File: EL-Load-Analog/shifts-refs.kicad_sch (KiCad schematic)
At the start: 44 parts, among them U501 TL431DBZ, U502 TL074, U503 TL074, U504 TL072

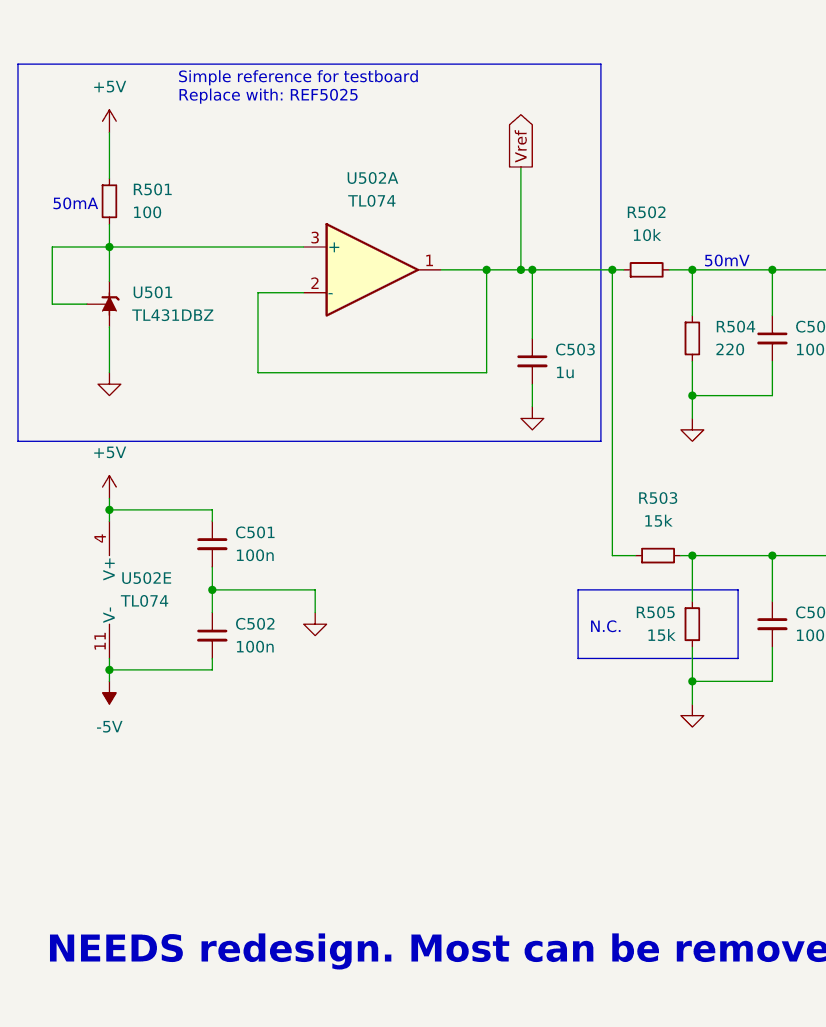
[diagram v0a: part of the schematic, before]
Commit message: Put REF2025 in place, added LICENSES and .gitignore
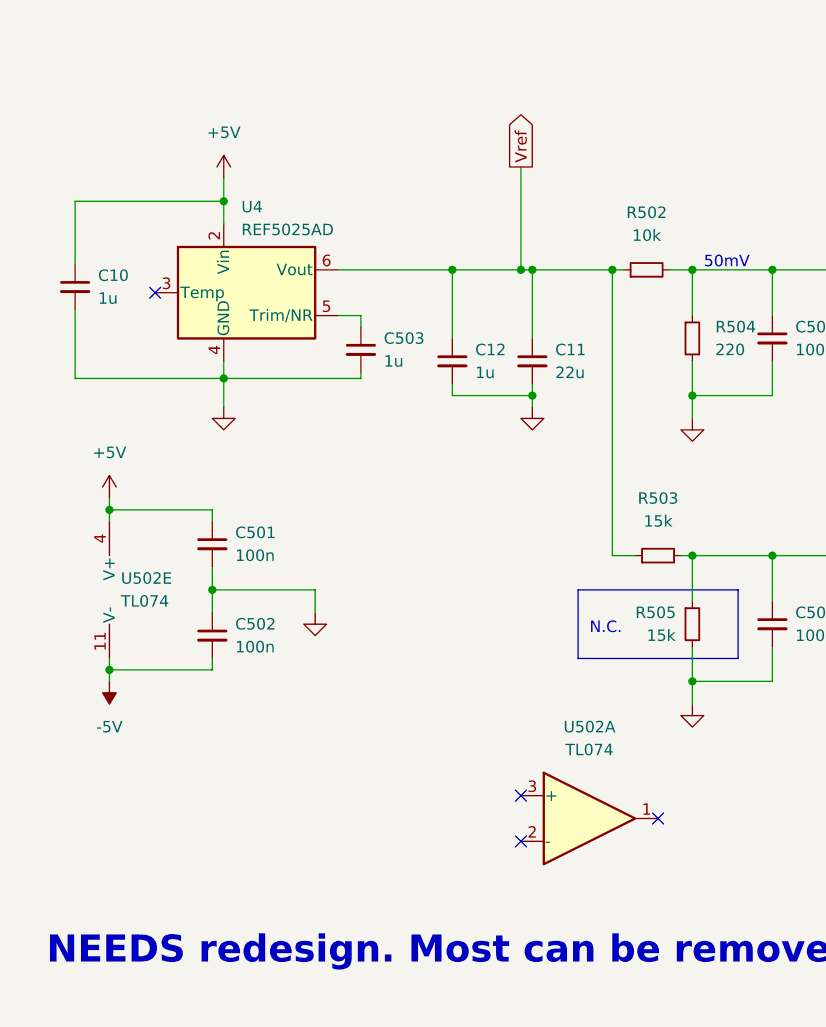
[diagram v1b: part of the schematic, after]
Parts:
- removed R501: 100, Resistor_SMD:R_0805_2012Metric_Pad1.20x1.40mm_HandSolder, symbol Device:R_Small
- removed U501: TL431DBZ, Package_TO_SOT_SMD:SOT-23, symbol Reference_Voltage:TL431DBZ
- added C10, C12: 1u, Capacitor_SMD:C_0805_2012Metric_Pad1.18x1.45mm_HandSolder, symbol Device:C_Small
- added C11: 22u, Capacitor_SMD:C_0805_2012Metric_Pad1.18x1.45mm_HandSolder, symbol Device:C_Small
- added U4: REF5025AD, Package_SO:SOIC-8_3.9x4.9mm_P1.27mm, symbol Reference_Voltage:REF5025AD
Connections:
- net +5V: now also C10.1, U4.2 (Vin)
- net GND: now also C10.2, C11.2, C12.2, U4.4 (GND)
- net Vref: now also C11.1, C12.1, U4.6 (Vout); no longer C503.1, U502.1, U502.2 (-)
- new net: C503.1, U4.5 (Trim/NR)
- no-connect marks 0 -> 4
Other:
- note removed: "50mA"
- note removed: "Simple reference for testboard Replace with: REF5025"
- moved on the sheet: C503, U502A

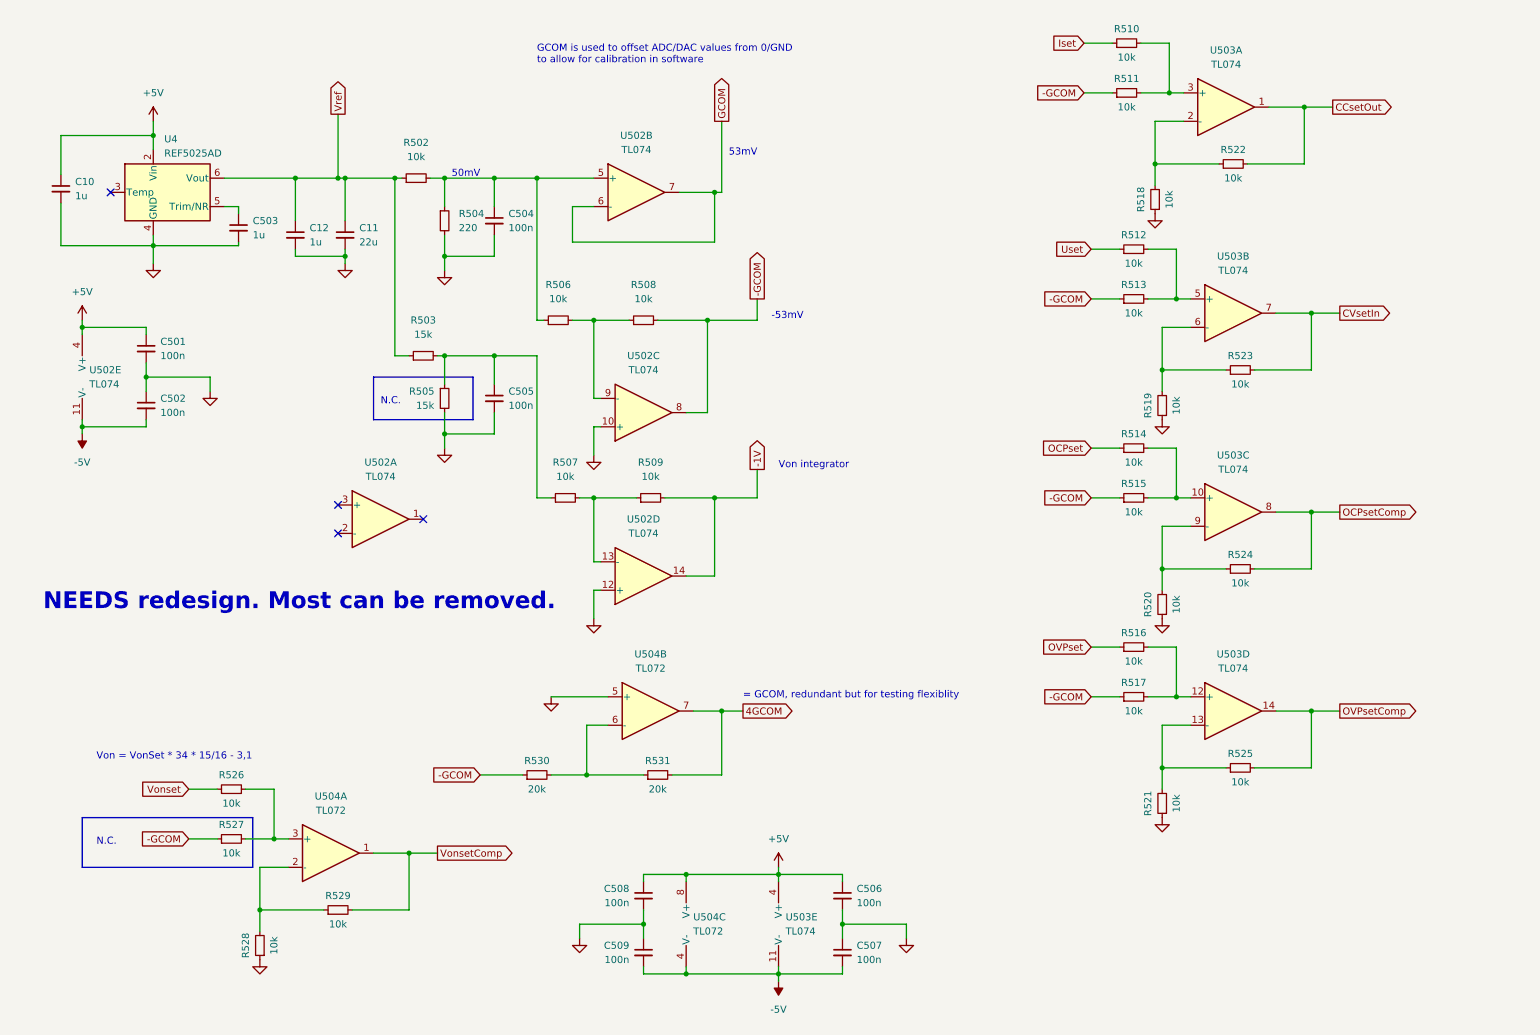
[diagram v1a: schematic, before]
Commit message: Major Analog PCB update DAC/ADC + connectors included, fan IC removed
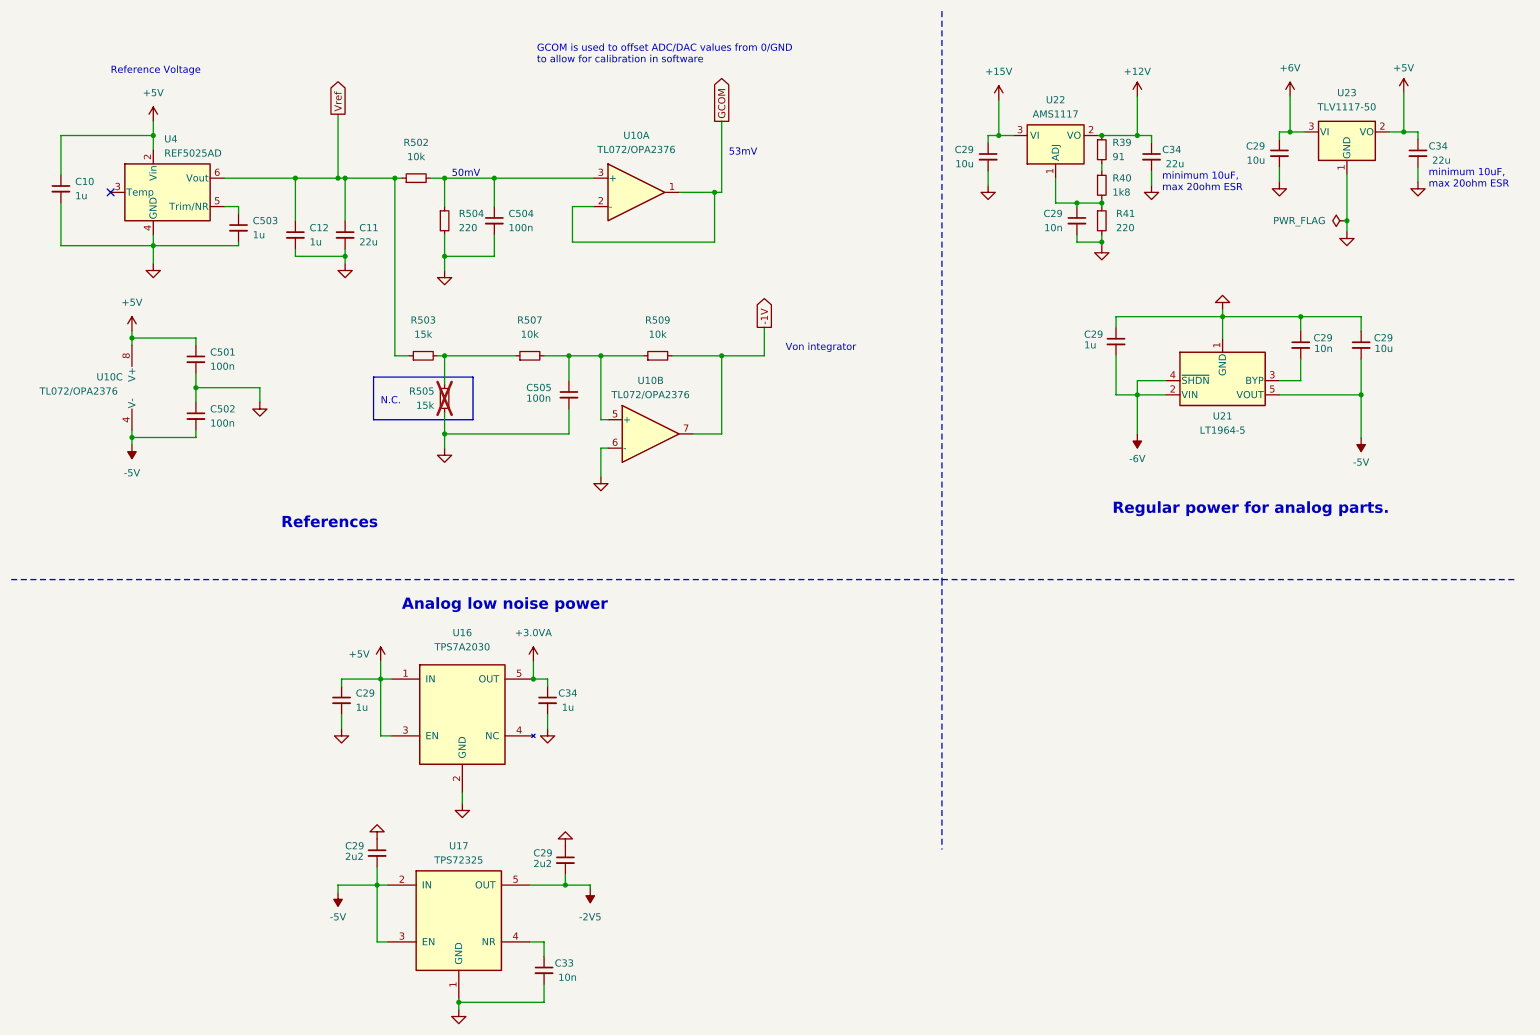
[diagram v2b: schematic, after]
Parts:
- removed C506, C507, C508, C509: 100n, Capacitor_SMD:C_0805_2012Metric_Pad1.18x1.45mm_HandSolder, symbol Device:C_Small
- removed R506, R508, R510, R511, R512, R513, R514, R515, R516, R517, R518, R519, R520, R521, R522, R523, R524, R525, R526, R527, R528, R529: 10k, Resistor_SMD:R_0805_2012Metric_Pad1.20x1.40mm_HandSolder, symbol Device:R_Small
- removed R530, R531: 20k, Resistor_SMD:R_0805_2012Metric_Pad1.20x1.40mm_HandSolder, symbol Device:R_Small
- removed U502, U503: TL074, Package_SO:SO-14_3.9x8.65mm_P1.27mm, symbol Amplifier_Operational:TL074
- removed U504: TL072, Package_SO:SO-8_3.9x4.9mm_P1.27mm, symbol Amplifier_Operational:TL072
- added C29 (x2): 2u2, Capacitor_SMD:C_0805_2012Metric, symbol Device:C_Small
- added C29 (x3): 10u, Capacitor_SMD:C_0805_2012Metric, symbol Device:C_Small
- added C29 (x2), C33: 10n, Capacitor_SMD:C_0805_2012Metric, symbol Device:C_Small
- added C29 (x2), C34: 1u, Capacitor_SMD:C_0805_2012Metric, symbol Device:C_Small
- added C34 (x2): 22u, Capacitor_SMD:C_0805_2012Metric, symbol Device:C_Small
- added R39: 91, Resistor_SMD:R_0805_2012Metric, symbol Device:R_Small
- added R40: 1k8, Resistor_SMD:R_0805_2012Metric, symbol Device:R_Small
- added R41: 220, Resistor_SMD:R_0805_2012Metric, symbol Device:R_Small
- added U10: TL072/OPA2376, Package_SO:SOIC-8_3.9x4.9mm_P1.27mm, symbol Amplifier_Operational:TL072
- added U16: TPS7A2030, Package_TO_SOT_SMD:SOT-23-5, symbol EL-Load-Digital-parts:TPS7A2030
- added U17: TPS72325, Package_TO_SOT_SMD:SOT-23-5, symbol EL-Load-Digital-parts:TPS72325
- added U21: LT1964-5, Package_TO_SOT_SMD:TSOT-23-5, symbol Regulator_Linear:LT1964-5
- added U22: AMS1117, Package_TO_SOT_SMD:SOT-223-3_TabPin2, symbol Regulator_Linear:AMS1117
- added U23: TLV1117-50, Package_TO_SOT_SMD:SOT-223-3_TabPin2, symbol Regulator_Linear:TLV1117-50
- C10, C11, C12, C501, C502, C503, C504, C505: footprint Capacitor_SMD:C_0805_2012Metric_Pad1.18x1.45mm_HandSolder -> Capacitor_SMD:C_0805_2012Metric
- R502, R503, R504, R507, R509: footprint Resistor_SMD:R_0805_2012Metric_Pad1.20x1.40mm_HandSolder -> Resistor_SMD:R_0805_2012Metric
- R505: footprint Resistor_SMD:R_0805_2012Metric_Pad1.20x1.40mm_HandSolder -> Resistor_SMD:R_0805_2012Metric; now not fitted; now left out of the parts list
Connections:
- net +5V: now also C29.1, C34.1, U10.8 (V+), U16.1 (IN), U16.3 (EN), U23.2 (VO)
- net -1V: now also U10.7
- net -5V: now also C29.2, C29.2, U10.4 (V-), U17.2 (IN), U17.3 (EN), U21.5 (VOUT)
- net GCOM: now also U10.1, U10.2 (-)
- net GND: now also C29.1, C29.1, C29.1, C29.1, C29.1, C29.2, C29.2, C29.2, C29.2, C33.2, C34.2, C34.2, C34.2, R41.2, U10.6 (-), U16.2 (GND), U17.1 (GND), U21.1 (GND), U23.1 (GND)
- net at R503.2, R505.1, R507.1: no longer C505.1
- net at R507.2, R509.1: now also C505.1, U10.5 (+)
- net at C504.1, R502.2, R504.1: now also U10.3 (+)
- new net: C33.1, U17.4 (NR)
- new net: C29.2, U21.3 (BYP)
- new net: C29.1, R40.2, R41.1, U22.1 (ADJ)
- new net: R39.2, R40.1
- new net +12V: C34.1, R39.1, U22.2 (VO)
- new net +15V: C29.1, U22.3 (VI)
- new net +3.0VA: C34.1, U16.5 (OUT)
- new net +6V: C29.1, U23.3 (VI)
- new net -2V5: C29.2, U17.5 (OUT)
- new net -6V: C29.2, U21.2 (VIN), U21.4 (~{SHDN})
- no-connect marks 4 -> 1
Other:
- note added: "Analog low noise power"
- note added: "Reference Voltage"
- note added: "References"
- note added: "Regular power for analog parts."
- note added: "minimum 10uF, max 20ohm ESR"
- note removed: "-53mV"
- note removed: "= GCOM, redundant but for testing flexiblity"
- note removed: "NEEDS redesign. Most can be removed."
- note removed: "Von = VonSet * 34 * 15/16 - 3,1"
- moved on the sheet: C501, C502, C505, R507, R509
